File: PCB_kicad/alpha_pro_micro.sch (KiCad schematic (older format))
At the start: 58 parts, among them J1 Conn_01x03, K1 KEYSW, K10 KEYSW, K11 KEYSW, K12 KEYSW, K13 KEYSW, K14 KEYSW, K15 KEYSW, K16 KEYSW, K17 KEYSW, K18 KEYSW, K19 KEYSW, K2 KEYSW, K20 KEYSW, K21 KEYSW, K22 KEYSW, K23 KEYSW, K24 KEYSW, K25 KEYSW, K26 KEYSW, K27 KEYSW, K28 KEYSW, K3 KEYSW, K4 KEYSW, K5 KEYSW, K6 KEYSW, K7 KEYSW, K8 KEYSW, K9 KEYSW, U1 ProMicro

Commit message: PCB v1.2!
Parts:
- added J2, J3, J4, J5, J6, J7, J8, J9: Conn_01x01_Female, Connector_PinHeader_2.54mm:PinHeader_1x01_P2.54mm_Vertical, symbol Connector:Conn_01x01_Female
- added SW1: SW_Push, random-keyboard-parts:SKQG-1155865, symbol Switch:SW_Push
- D1, D10, D11, D12, D13, D14, D15, D16, D17, D18, D19, D2, D20, D21, D22, D23, D24, D25, D26, D27, D28, D3, D4, D5, D6, D7, D8, D9: footprint Diodes_THT:D_DO-35_SOD27_P7.62mm_Horizontal -> combodiode:ComboDiode
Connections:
- net GND: now also SW1.2
- net row0: now also J2.1 (Pin_1), J3.1 (Pin_1)
- net row1: now also J4.1 (Pin_1), J5.1 (Pin_1)
- net row2: now also J6.1 (Pin_1), J7.1 (Pin_1)
- net RGB: now reaches J1.2 (Pin_2), U1.20 (F4)
- net RST: now reaches U1.22 (RST)
- net RST: now also SW1.1
- net col_tmo: now reaches U1.5 (SCL)
- net col_tmo: now also J8.1 (Pin_1), J9.1 (Pin_1)
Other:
- moved on the sheet: J1

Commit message: Alpha v2.0 released!
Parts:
- K1, K10, K11, K12, K13, K14, K15, K16, K17, K18, K19, K2, K20, K21, K22, K23, K24, K26, K27, K28, K3, K4, K5, K6, K7, K8, K9: footprint MX_Alps_Hybrid:MX-1U-NoLED -> keebio-parts:MX-Alps-Choc-1U-NoLED
- K25: footprint MX_Alps_Hybrid:MX-2U-ReversedStabilizers-NoLED -> keebio-parts:MX-Alps-Choc-2U-StabFlip
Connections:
- net col0: now also K1.2, K11.2, K21.2; no longer K1.1, K11.1, K21.1
- net col1: now also K12.2, K2.2, K22.2; no longer K12.1, K2.1, K22.1
- net col2: now also K13.2, K23.2, K3.2; no longer K13.1, K23.1, K3.1
- net col3: now also K14.2, K24.2, K4.2; no longer K14.1, K24.1, K4.1
- net col4: now also K15.2, K5.2; no longer K15.1, K5.1
- net col5: now also K16.2, K6.2; no longer K16.1, K6.1
- net col6: now also K17.2, K7.2; no longer K17.1, K7.1
- net col7: now also K18.2, K26.2, K8.2; no longer K18.1, K26.1, K8.1
- net col8: now also K19.2, K27.2, K9.2; no longer K19.1, K27.1, K9.1
- net col9: now also K10.2, K20.2, K28.2; no longer K10.1, K20.1, K28.1
- net at D2.2 (A): now also K2.1; no longer K2.2
- net at D1.2 (A): now also K1.1; no longer K1.2
- net at D3.2 (A): now also K3.1; no longer K3.2
- net at D11.2 (A): now also K11.1; no longer K11.2
- net at D12.2 (A): now also K12.1; no longer K12.2
- net at D13.2 (A): now also K13.1; no longer K13.2
- net at D4.2 (A): now also K4.1; no longer K4.2
- net at D14.2 (A): now also K14.1; no longer K14.2
- net at D15.2 (A): now also K15.1; no longer K15.2
- net at D16.2 (A): now also K16.1; no longer K16.2
- net at D5.2 (A): now also K5.1; no longer K5.2
- net at D6.2 (A): now also K6.1; no longer K6.2
- net at D21.2 (A): now also K21.1; no longer K21.2
- net at D22.2 (A): now also K22.1; no longer K22.2
- net at D23.2 (A): now also K23.1; no longer K23.2
- net at D24.2 (A): now also K24.1; no longer K24.2
- net at D27.2 (A): now also K27.1; no longer K27.2
- net at D7.2 (A): now also K7.1; no longer K7.2
- net at D8.2 (A): now also K8.1; no longer K8.2
- net at D9.2 (A): now also K9.1; no longer K9.2
- net at D10.2 (A): now also K10.1; no longer K10.2
- net at D17.2 (A): now also K17.1; no longer K17.2
- net at D18.2 (A): now also K18.1; no longer K18.2
- net at D19.2 (A): now also K19.1; no longer K19.2
- net at D20.2 (A): now also K20.1; no longer K20.2
- net at D26.2 (A): now also K26.1; no longer K26.2
- net at D28.2 (A): now also K28.1; no longer K28.2
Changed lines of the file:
@@
 F 0 "K11" H 1150 4400 60  0000 C CNN
 F 1 "KEYSW" H 1200 4300 60  0001 C CNN
-F 2 "MX_Alps_Hybrid:MX-1U-NoLED" H 1200 4400 60  0001 C CNN
+F 2 "keebio-parts:MX-Alps-Choc-1U-NoLED" H 1200 4400 60  0001 C CNN
 F 3 "" H 1200 4400 60  0000 C CNN
 	1    1200 4400
-	1    0    0    -1
+	-1   0    0    -1
 $EndComp
 $Comp
@@
 F 0 "K12" H 2100 4400 60  0000 C CNN
 F 1 "KEYSW" H 2150 4300 60  0001 C CNN
-F 2 "MX_Alps_Hybrid:MX-1U-NoLED" H 2150 4400 60  0001 C CNN
+F 2 "keebio-parts:MX-Alps-Choc-1U-NoLED" H 2150 4400 60  0001 C CNN
 F 3 "" H 2150 4400 60  0000 C CNN
 	1    2150 4400
-	1    0    0    -1
+	-1   0    0    -1
 $EndComp
 $Comp
@@
 F 0 "K13" H 3050 4450 60  0000 C CNN
 F 1 "KEYSW" H 3100 4350 60  0001 C CNN
-F 2 "MX_Alps_Hybrid:MX-1U-NoLED" H 3100 4450 60  0001 C CNN
+F 2 "keebio-parts:MX-Alps-Choc-1U-NoLED" H 3100 4450 60  0001 C CNN
 F 3 "" H 3100 4450 60  0000 C CNN
 	1    3100 4450
-	1    0    0    -1
+	-1   0    0    -1
 $EndComp
 $Comp
@@
 F 0 "K14" H 4150 4450 60  0000 C CNN
 F 1 "KEYSW" H 4200 4350 60  0001 C CNN
-F 2 "MX_Alps_Hybrid:MX-1U-NoLED" H 4200 4450 60  0001 C CNN
+F 2 "keebio-parts:MX-Alps-Choc-1U-NoLED" H 4200 4450 60  0001 C CNN
 F 3 "" H 4200 4450 60  0000 C CNN
 	1    4200 4450
-	1    0    0    -1
+	-1   0    0    -1
 $EndComp
 $Comp
@@
 F 0 "K15" H 5050 4450 60  0000 C CNN
 F 1 "KEYSW" H 5100 4350 60  0001 C CNN
-F 2 "MX_Alps_Hybrid:MX-1U-NoLED" H 5100 4450 60  0001 C CNN
+F 2 "keebio-parts:MX-Alps-Choc-1U-NoLED" H 5100 4450 60  0001 C CNN
 F 3 "" H 5100 4450 60  0000 C CNN
 	1    5100 4450
-	1    0    0    -1
+	-1   0    0    -1
 $EndComp
 $Comp
@@
 F 0 "K16" H 5900 4450 60  0000 C CNN
 F 1 "KEYSW" H 5950 4350 60  0001 C CNN
-F 2 "MX_Alps_Hybrid:MX-1U-NoLED" H 5950 4450 60  0001 C CNN
+F 2 "keebio-parts:MX-Alps-Choc-1U-NoLED" H 5950 4450 60  0001 C CNN
 F 3 "" H 5950 4450 60  0000 C CNN
 	1    5950 4450
-	1    0    0    -1
+	-1   0    0    -1
 $EndComp
 $Comp
@@
 F 0 "K21" H 1750 5150 60  0000 C CNN
 F 1 "KEYSW" H 1800 5050 60  0001 C CNN
-F 2 "MX_Alps_Hybrid:MX-1U-NoLED" H 1800 5150 60  0001 C CNN
+F 2 "keebio-parts:MX-Alps-Choc-1U-NoLED" H 1800 5150 60  0001 C CNN
 F 3 "" H 1800 5150 60  0000 C CNN
 	1    1800 5150
-	1    0    0    -1
+	-1   0    0    -1
 $EndComp
 $Comp
@@
 F 0 "K22" H 2650 5150 60  0000 C CNN
 F 1 "KEYSW" H 2700 5050 60  0001 C CNN
-F 2 "MX_Alps_Hybrid:MX-1U-NoLED" H 2700 5150 60  0001 C CNN
+F 2 "keebio-parts:MX-Alps-Choc-1U-NoLED" H 2700 5150 60  0001 C CNN
 F 3 "" H 2700 5150 60  0000 C CNN
 	1    2700 5150
-	1    0    0    -1
+	-1   0    0    -1
 $EndComp
 $Comp
@@
 F 0 "K23" H 3600 5150 60  0000 C CNN
 F 1 "KEYSW" H 3650 5050 60  0001 C CNN
-F 2 "MX_Alps_Hybrid:MX-1U-NoLED" H 3650 5150 60  0001 C CNN
+F 2 "keebio-parts:MX-Alps-Choc-1U-NoLED" H 3650 5150 60  0001 C CNN
 F 3 "" H 3650 5150 60  0000 C CNN
 	1    3650 5150
-	1    0    0    -1
+	-1   0    0    -1
 $EndComp
 $Comp
@@
 F 0 "K24" H 4650 5150 60  0000 C CNN
 F 1 "KEYSW" H 4700 5050 60  0001 C CNN
-F 2 "MX_Alps_Hybrid:MX-1U-NoLED" H 4700 5150 60  0001 C CNN
+F 2 "keebio-parts:MX-Alps-Choc-1U-NoLED" H 4700 5150 60  0001 C CNN
 F 3 "" H 4700 5150 60  0000 C CNN
 	1    4700 5150
-	1    0    0    -1
+	-1   0    0    -1
 $EndComp
 $Comp
@@
 F 0 "K25" H 5900 5150 60  0000 C CNN
 F 1 "KEYSW" H 5950 5050 60  0001 C CNN
-F 2 "MX_Alps_Hybrid:MX-2U-ReversedStabilizers-NoLED" H 5950 5150 60  0001 C CNN
+F 2 "keebio-parts:MX-Alps-Choc-2U-StabFlip" H 5950 5150 60  0001 C CNN
 F 3 "" H 5950 5150 60  0000 C CNN
 	1    5950 5150
@@
 F 0 "K27" H 8500 5150 60  0000 C CNN
 F 1 "KEYSW" H 8550 5050 60  0001 C CNN
-F 2 "MX_Alps_Hybrid:MX-1U-NoLED" H 8550 5150 60  0001 C CNN
+F 2 "keebio-parts:MX-Alps-Choc-1U-NoLED" H 8550 5150 60  0001 C CNN
 F 3 "" H 8550 5150 60  0000 C CNN
 	1    8550 5150
-	1    0    0    -1
+	-1   0    0    -1
 $EndComp
 $Comp
@@
 F 0 "K9" H 9050 3700 60  0000 C CNN
 F 1 "KEYSW" H 9100 3600 60  0001 C CNN
-F 2 "MX_Alps_Hybrid:MX-1U-NoLED" H 9100 3700 60  0001 C CNN
+F 2 "keebio-parts:MX-Alps-Choc-1U-NoLED" H 9100 3700 60  0001 C CNN
 F 3 "" H 9100 3700 60  0000 C CNN
 	1    9100 3700
-	1    0    0    -1
+	-1   0    0    -1
 $EndComp
 $Comp
@@
 F 0 "K10" H 10000 3700 60  0000 C CNN
 F 1 "KEYSW" H 10050 3600 60  0001 C CNN
-F 2 "MX_Alps_Hybrid:MX-1U-NoLED" H 10050 3700 60  0001 C CNN
+F 2 "keebio-parts:MX-Alps-Choc-1U-NoLED" H 10050 3700 60  0001 C CNN
 F 3 "" H 10050 3700 60  0000 C CNN
 	1    10050 3700
-	1    0    0    -1
+	-1   0    0    -1
 $EndComp
 $Comp
@@
 F 0 "K17" H 7100 4500 60  0000 C CNN
 F 1 "KEYSW" H 7150 4400 60  0001 C CNN
-F 2 "MX_Alps_Hybrid:MX-1U-NoLED" H 7150 4500 60  0001 C CNN
+F 2 "keebio-parts:MX-Alps-Choc-1U-NoLED" H 7150 4500 60  0001 C CNN
 F 3 "" H 7150 4500 60  0000 C CNN
 	1    7150 4500
-	1    0    0    -1
+	-1   0    0    -1
 $EndComp
 $Comp
@@
 F 0 "K18" H 8050 4500 60  0000 C CNN
 F 1 "KEYSW" H 8100 4400 60  0001 C CNN
-F 2 "MX_Alps_Hybrid:MX-1U-NoLED" H 8100 4500 60  0001 C CNN
+F 2 "keebio-parts:MX-Alps-Choc-1U-NoLED" H 8100 4500 60  0001 C CNN
 F 3 "" H 8100 4500 60  0000 C CNN
 	1    8100 4500
-	1    0    0    -1
+	-1   0    0    -1
 $EndComp
 $Comp
@@
 F 0 "K19" H 9050 4500 60  0000 C CNN
 F 1 "KEYSW" H 9100 4400 60  0001 C CNN
-F 2 "MX_Alps_Hybrid:MX-1U-NoLED" H 9100 4500 60  0001 C CNN
+F 2 "keebio-parts:MX-Alps-Choc-1U-NoLED" H 9100 4500 60  0001 C CNN
 F 3 "" H 9100 4500 60  0000 C CNN
 	1    9100 4500
-	1    0    0    -1
+	-1   0    0    -1
 $EndComp
 $Comp
@@
 F 0 "K20" H 10000 4500 60  0000 C CNN
 F 1 "KEYSW" H 10050 4400 60  0001 C CNN
-F 2 "MX_Alps_Hybrid:MX-1U-NoLED" H 10050 4500 60  0001 C CNN
+F 2 "keebio-parts:MX-Alps-Choc-1U-NoLED" H 10050 4500 60  0001 C CNN
 F 3 "" H 10050 4500 60  0000 C CNN
 	1    10050 4500
-	1    0    0    -1
+	-1   0    0    -1
 $EndComp
 $Comp
@@
 F 0 "K26" H 7400 5150 60  0000 C CNN
 F 1 "KEYSW" H 7450 5050 60  0001 C CNN
-F 2 "MX_Alps_Hybrid:MX-1U-NoLED" H 7450 5150 60  0001 C CNN
+F 2 "keebio-parts:MX-Alps-Choc-1U-NoLED" H 7450 5150 60  0001 C CNN
 F 3 "" H 7450 5150 60  0000 C CNN
 	1    7450 5150
-	1    0    0    -1
+	-1   0    0    -1
 $EndComp
 $Comp
@@
 F 0 "K28" H 9500 5150 60  0000 C CNN
 F 1 "KEYSW" H 9550 5050 60  0001 C CNN
-F 2 "MX_Alps_Hybrid:MX-1U-NoLED" H 9550 5150 60  0001 C CNN
+F 2 "keebio-parts:MX-Alps-Choc-1U-NoLED" H 9550 5150 60  0001 C CNN
 F 3 "" H 9550 5150 60  0000 C CNN
 	1    9550 5150
-	1    0    0    -1
+	-1   0    0    -1
 $EndComp
 $Comp
@@
 F 0 "K8" H 8050 3700 60  0000 C CNN
 F 1 "KEYSW" H 8100 3600 60  0001 C CNN
-F 2 "MX_Alps_Hybrid:MX-1U-NoLED" H 8100 3700 60  0001 C CNN
+F 2 "keebio-parts:MX-Alps-Choc-1U-NoLED" H 8100 3700 60  0001 C CNN
 F 3 "" H 8100 3700 60  0000 C CNN
 	1    8100 3700
-	1    0    0    -1
+	-1   0    0    -1
 $EndComp
 $Comp
@@
 F 0 "K7" H 7100 3700 60  0000 C CNN
 F 1 "KEYSW" H 7150 3600 60  0001 C CNN
-F 2 "MX_Alps_Hybrid:MX-1U-NoLED" H 7150 3700 60  0001 C CNN
+F 2 "keebio-parts:MX-Alps-Choc-1U-NoLED" H 7150 3700 60  0001 C CNN
 F 3 "" H 7150 3700 60  0000 C CNN
 	1    7150 3700
-	1    0    0    -1
+	-1   0    0    -1
 $EndComp
 $Comp
@@
 F 0 "K6" H 6050 3700 60  0000 C CNN
 F 1 "KEYSW" H 6100 3600 60  0001 C CNN
-F 2 "MX_Alps_Hybrid:MX-1U-NoLED" H 6100 3700 60  0001 C CNN
+F 2 "keebio-parts:MX-Alps-Choc-1U-NoLED" H 6100 3700 60  0001 C CNN
 F 3 "" H 6100 3700 60  0000 C CNN
 	1    6100 3700
-	1    0    0    -1
+	-1   0    0    -1
 $EndComp
 $Comp
@@
 F 0 "K5" H 5100 3700 60  0000 C CNN
 F 1 "KEYSW" H 5150 3600 60  0001 C CNN
-F 2 "MX_Alps_Hybrid:MX-1U-NoLED" H 5150 3700 60  0001 C CNN
+F 2 "keebio-parts:MX-Alps-Choc-1U-NoLED" H 5150 3700 60  0001 C CNN
 F 3 "" H 5150 3700 60  0000 C CNN
 	1    5150 3700
-	1    0    0    -1
+	-1   0    0    -1
 $EndComp
 $Comp
@@
 F 0 "K4" H 4150 3650 60  0000 C CNN
 F 1 "KEYSW" H 4200 3550 60  0001 C CNN
-F 2 "MX_Alps_Hybrid:MX-1U-NoLED" H 4200 3650 60  0001 C CNN
+F 2 "keebio-parts:MX-Alps-Choc-1U-NoLED" H 4200 3650 60  0001 C CNN
 F 3 "" H 4200 3650 60  0000 C CNN
 	1    4200 3650
-	1    0    0    -1
+	-1   0    0    -1
 $EndComp
 $Comp
@@
 F 0 "K3" H 3100 3650 60  0000 C CNN
 F 1 "KEYSW" H 3150 3550 60  0001 C CNN
-F 2 "MX_Alps_Hybrid:MX-1U-NoLED" H 3150 3650 60  0001 C CNN
+F 2 "keebio-parts:MX-Alps-Choc-1U-NoLED" H 3150 3650 60  0001 C CNN
 F 3 "" H 3150 3650 60  0000 C CNN
 	1    3150 3650
-	1    0    0    -1
+	-1   0    0    -1
 $EndComp
 $Comp
@@
 F 0 "K2" H 2100 3650 60  0000 C CNN
 F 1 "KEYSW" H 2150 3550 60  0001 C CNN
-F 2 "MX_Alps_Hybrid:MX-1U-NoLED" H 2150 3650 60  0001 C CNN
+F 2 "keebio-parts:MX-Alps-Choc-1U-NoLED" H 2150 3650 60  0001 C CNN
 F 3 "" H 2150 3650 60  0000 C CNN
 	1    2150 3650
-	1    0    0    -1
+	-1   0    0    -1
 $EndComp
 $Comp
@@
 F 0 "K1" H 1200 3650 60  0000 C CNN
 F 1 "KEYSW" H 1250 3550 60  0001 C CNN
-F 2 "MX_Alps_Hybrid:MX-1U-NoLED" H 1250 3650 60  0001 C CNN
+F 2 "keebio-parts:MX-Alps-Choc-1U-NoLED" H 1250 3650 60  0001 C CNN
 F 3 "" H 1250 3650 60  0000 C CNN
 	1    1250 3650
-	1    0    0    -1
-$EndComp
-Wire Wire Line
+	-1   0    0    -1
+$EndComp
+Wire Wire Line

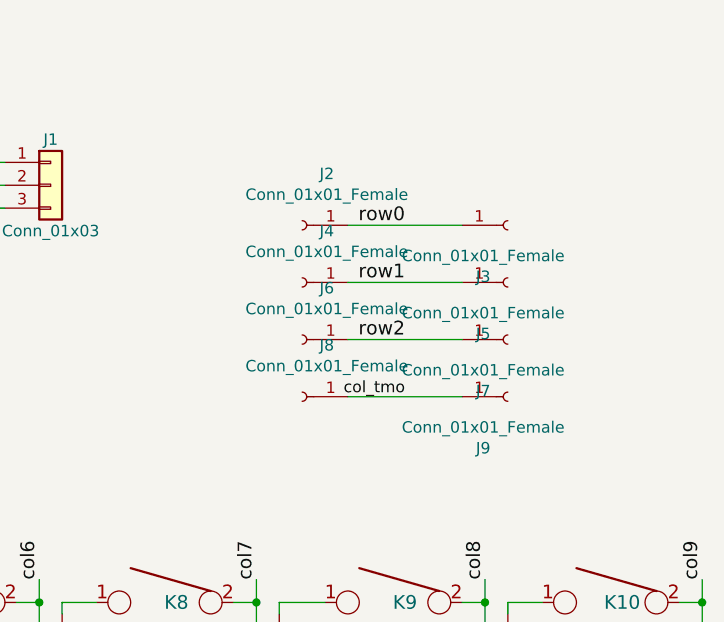
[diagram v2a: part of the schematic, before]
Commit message: removed tmo28 breakouts
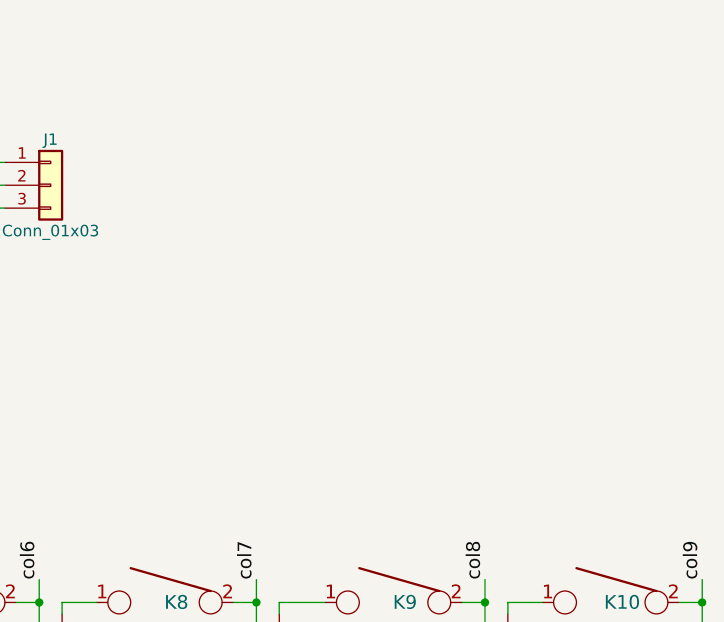
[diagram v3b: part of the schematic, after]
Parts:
- removed J2, J3, J4, J5, J6, J7, J8, J9: Conn_01x01_Female, Connector_PinHeader_2.54mm:PinHeader_1x01_P2.54mm_Vertical, symbol Connector:Conn_01x01_Female
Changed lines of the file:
@@
 Text GLabel 5400 1850 2    50   Input ~ 0
 RGB
-$Comp
-L Connector:Conn_01x01_Female J2
-U 1 1 5CC5F73A
-P 8700 2050
-F 0 "J2" H 8592 1825 50  0000 C CNN
-F 1 "Conn_01x01_Female" H 8592 1916 50  0000 C CNN
-F 2 "Connector_PinHeader_2.54mm:PinHeader_1x01_P2.54mm_Vertical" H 8700 2050 50  0001 C CNN
-F 3 "~" H 8700 2050 50  0001 C CNN
-	1    8700 2050
-	-1   0    0    1
-$EndComp
-$Comp
-L Connector:Conn_01x01_Female J4
-U 1 1 5CC5FD0E
-P 8700 2300
-F 0 "J4" H 8592 2075 50  0000 C CNN
-F 1 "Conn_01x01_Female" H 8592 2166 50  0000 C CNN
-F 2 "Connector_PinHeader_2.54mm:PinHeader_1x01_P2.54mm_Vertical" H 8700 2300 50  0001 C CNN
-F 3 "~" H 8700 2300 50  0001 C CNN
-	1    8700 2300
-	-1   0    0    1
-$EndComp
-$Comp
-L Connector:Conn_01x01_Female J6
-U 1 1 5CC60365
-P 8700 2550
-F 0 "J6" H 8592 2325 50  0000 C CNN
-F 1 "Conn_01x01_Female" H 8592 2416 50  0000 C CNN
-F 2 "Connector_PinHeader_2.54mm:PinHeader_1x01_P2.54mm_Vertical" H 8700 2550 50  0001 C CNN
-F 3 "~" H 8700 2550 50  0001 C CNN
-	1    8700 2550
-	-1   0    0    1
-$EndComp
-$Comp
-L Connector:Conn_01x01_Female J8
-U 1 1 5CC607D9
-P 8700 2800
-F 0 "J8" H 8592 2575 50  0000 C CNN
-F 1 "Conn_01x01_Female" H 8592 2666 50  0000 C CNN
-F 2 "Connector_PinHeader_2.54mm:PinHeader_1x01_P2.54mm_Vertical" H 8700 2800 50  0001 C CNN
-F 3 "~" H 8700 2800 50  0001 C CNN
-	1    8700 2800
-	-1   0    0    1
-$EndComp
-Text Label 9150 2050 2    60   ~ 0
-row0
-Text Label 9150 2300 2    60   ~ 0
-row1
-Text Label 9150 2550 2    60   ~ 0
-row2
-Text Label 9150 2800 2    50   ~ 0
-col_tmo
-$Comp
-L Connector:Conn_01x01_Female J9
-U 1 1 5CC8D43F
-P 9600 2800
-F 0 "J9" H 9492 2575 50  0000 C CNN
-F 1 "Conn_01x01_Female" H 9492 2666 50  0000 C CNN
-F 2 "Connector_PinHeader_2.54mm:PinHeader_1x01_P2.54mm_Vertical" H 9600 2800 50  0001 C CNN
-F 3 "~" H 9600 2800 50  0001 C CNN
-	1    9600 2800
-	1    0    0    -1
-$EndComp
-$Comp
-L Connector:Conn_01x01_Female J7
-U 1 1 5CC8D449
-P 9600 2550
-F 0 "J7" H 9492 2325 50  0000 C CNN
-F 1 "Conn_01x01_Female" H 9492 2416 50  0000 C CNN
-F 2 "Connector_PinHeader_2.54mm:PinHeader_1x01_P2.54mm_Vertical" H 9600 2550 50  0001 C CNN
-F 3 "~" H 9600 2550 50  0001 C CNN
-	1    9600 2550
-	1    0    0    -1
-$EndComp
-$Comp
-L Connector:Conn_01x01_Female J5
-U 1 1 5CC8D453
-P 9600 2300
-F 0 "J5" H 9492 2075 50  0000 C CNN
-F 1 "Conn_01x01_Female" H 9492 2166 50  0000 C CNN
-F 2 "Connector_PinHeader_2.54mm:PinHeader_1x01_P2.54mm_Vertical" H 9600 2300 50  0001 C CNN
-F 3 "~" H 9600 2300 50  0001 C CNN
-	1    9600 2300
-	1    0    0    -1
-$EndComp
-$Comp
-L Connector:Conn_01x01_Female J3
-U 1 1 5CC8D45D
-P 9600 2050
-F 0 "J3" H 9492 1825 50  0000 C CNN
-F 1 "Conn_01x01_Female" H 9492 1916 50  0000 C CNN
-F 2 "Connector_PinHeader_2.54mm:PinHeader_1x01_P2.54mm_Vertical" H 9600 2050 50  0001 C CNN
-F 3 "~" H 9600 2050 50  0001 C CNN
-	1    9600 2050
-	1    0    0    -1
-$EndComp
-Wire Wire Line
-	9400 2050 8900 2050
-Wire Wire Line
-	8900 2300 9400 2300
-Wire Wire Line
-	8900 2550 9400 2550
-Wire Wire Line
-	8900 2800 9400 2800
 Text Label 4000 1850 2    50   ~ 0
 col_tmo
